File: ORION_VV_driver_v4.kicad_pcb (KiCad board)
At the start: 4 copper layers, 52.4 x 123.1 mm, 154 parts, among them J1 Conn_01x01, J10 Conn_01x01, J11 Conn_01x02, J12 Conn_01x05, J13 Conn_01x05, J14 Conn_01x01, J15 Conn_01x02, J16 Conn_01x01, J17 Conn_01x01, J18 Conn_01x01, J19 Conn_01x01, J2 Conn_01x04, J3 Conn_01x04, J4 Conn_01x06, J5 Conn_01x07, J6 Conn_01x07, J7 Conn_01x01, J8 Conn_01x01, J9 Conn_01x01, Q1 IRF8721PBF-1, Q10 IRF8721PBF-1, Q11 IRF8721PBF-1, Q12 IRF8721PBF-1, Q2 IRF8721PBF-1, Q3 IRF8721PBF-1, Q4 IRF8721PBF-1, Q5 IRF8721PBF-1, Q6 IRF8721PBF-1, Q7 IRF8721PBF-1, Q8 IRF8721PBF-1, Q9 IRF8721PBF-1, SW1 SW_Push, SW2 SW_Push, SW3 SW_Push, SW4 SW_Push, SW5 SW_Push, U1 BD9G101G, U2 L78L33_SOT89, U3 MAX3051, U5 ZXCT108x, U6 ZXCT108x, Y1 Resonator

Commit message: DRC通ってるか！？？！？
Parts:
- SW1, SW2, SW3, SW4, SW5: footprint Button_Switch_SMD:SW_Push_1P1T_NO_CK_KMR2 -> Button_Switch_SMD:SW_Push_SPST_NO_Alps_SKRK
- moved R7 1.80 mm to (115.5, 109.8)
- moved C52 0.94 mm to (108.7, 90.6)
- moved R11 0.82 mm to (113.0, 90.5)
- moved C16 0.81 mm to (113.0, 89.5)
- moved Y1 0.81 mm to (109.5, 107.5)
- turned SW2 to 90 degrees
- turned SW3 to 90 degrees
- turned SW4 to 90 degrees
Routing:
- net GND: track 169.4 -> 203.9 mm, vias 164 -> 176
- net +3V3: track 166.8 -> 187.3 mm, vias 4 -> 5
- net /LED_0: track 1.74 -> 15.6 mm
- net /LED_1: track 1.24 -> 12.8 mm
- net /LED_2: track 0.57 -> 12.0 mm
- net +BATT: track 59.4 -> 48.2 mm, vias 19 -> 18
- net /SW3: track 34.5 -> 29.6 mm
- net /NRST: track 43.4 -> 38.9 mm
- net /SW1: track 37.5 -> 33.5 mm
- net /SW0: track 40.5 -> 36.7 mm
- net /SW2: track 35.4 -> 32.1 mm
- net +9V: track 192.7 -> 195.9 mm, vias 9 -> 10
- net /BATT_V_SENS: track 9.55 -> 8.23 mm
- net /M1_CS: track 35.2 -> 34.1 mm
- net Net-(R7-Pad2): track 8.42 -> 7.26 mm
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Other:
- board text added: "V4.3"
- board text removed: "V4.2"

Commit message: パワー系チェック用のテストパッド追加
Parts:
- added J20: Conn_01x01, TestPoint:TestPoint_Loop_D2.60mm_Drill0.9mm_Beaded, F.Cu at (137.5, 94.5)
- added J21: Conn_01x01, TestPoint:TestPoint_Loop_D2.60mm_Drill0.9mm_Beaded, F.Cu at (137.5, 105.5)
- added J22: Conn_01x01, TestPoint:TestPoint_Loop_D2.60mm_Drill0.9mm_Beaded, F.Cu at (131.0, 130.5)
- added J23: Conn_01x01, TestPoint:TestPoint_Loop_D2.60mm_Drill0.9mm_Beaded, F.Cu at (131.0, 69.5)
- SW1, SW2, SW3, SW4, SW5: footprint Button_Switch_SMD:SW_Push_SPST_NO_Alps_SKRK -> Button_Switch_SMD:SW_Push_1P1T_NO_CK_KMR2
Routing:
- net GND: track 203.9 -> 274.1 mm, vias 176 -> 178
- net /SW0: track 36.7 -> 0.00 mm, vias 1 -> 0
- net /SW1: track 33.5 -> 0.00 mm, vias 1 -> 0
- net /M1_CSL: vias 169 -> 163
- net /M0_CSL: vias 168 -> 162
- added copper zone on B.Cu, net +BATT
- added copper zone on In1.Cu, net +BATT
- added copper zone on In2.Cu, net +BATT

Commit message: 盆栽
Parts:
- SW1, SW2, SW3, SW4, SW5: footprint Button_Switch_SMD:SW_Push_1P1T_NO_CK_KMR2 -> Button_Switch_SMD:SW_Push_SPST_NO_Alps_SKRK
- moved SW2 1.75 mm to (118.5, 128.0)
- moved SW3 1.75 mm to (115.0, 128.0)
- moved SW4 1.75 mm to (111.5, 128.0)
- moved SW5 1.75 mm to (108.0, 128.0)
- moved R10 0.40 mm to (119.5, 92.4)
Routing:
- net GND: track 274.1 -> 204.3 mm, vias 178 -> 176
- net /SW0: track 0.00 -> 35.1 mm, vias 0 -> 1
- net /SW1: track 0.00 -> 32.1 mm, vias 0 -> 1
- net /SW2: track 32.1 -> 30.1 mm
- net /M0_CSL: track 5.91 -> 7.31 mm
- net +9V: track 195.9 -> 197.0 mm
- net /SW3: track 29.6 -> 28.9 mm

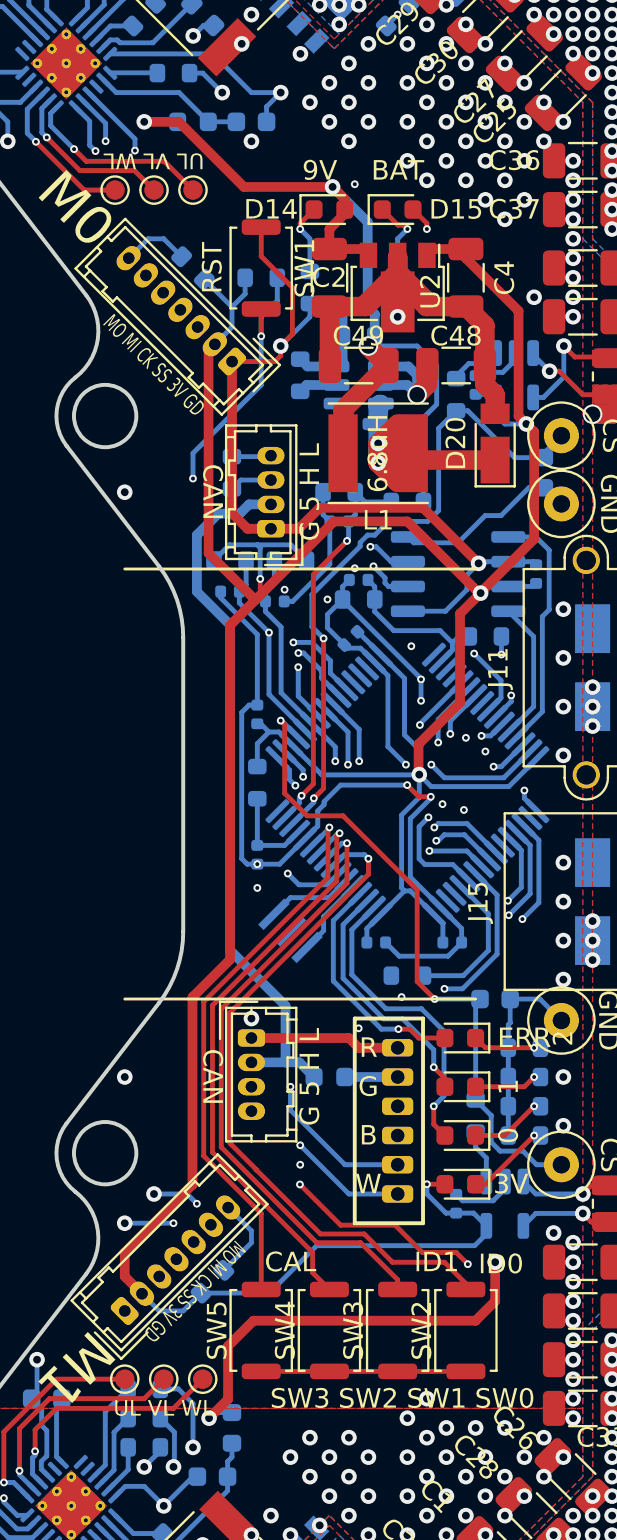
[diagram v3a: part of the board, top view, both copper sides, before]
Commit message: エンコーダ電源にFB追加、GD電源に0Ω抵抗追加
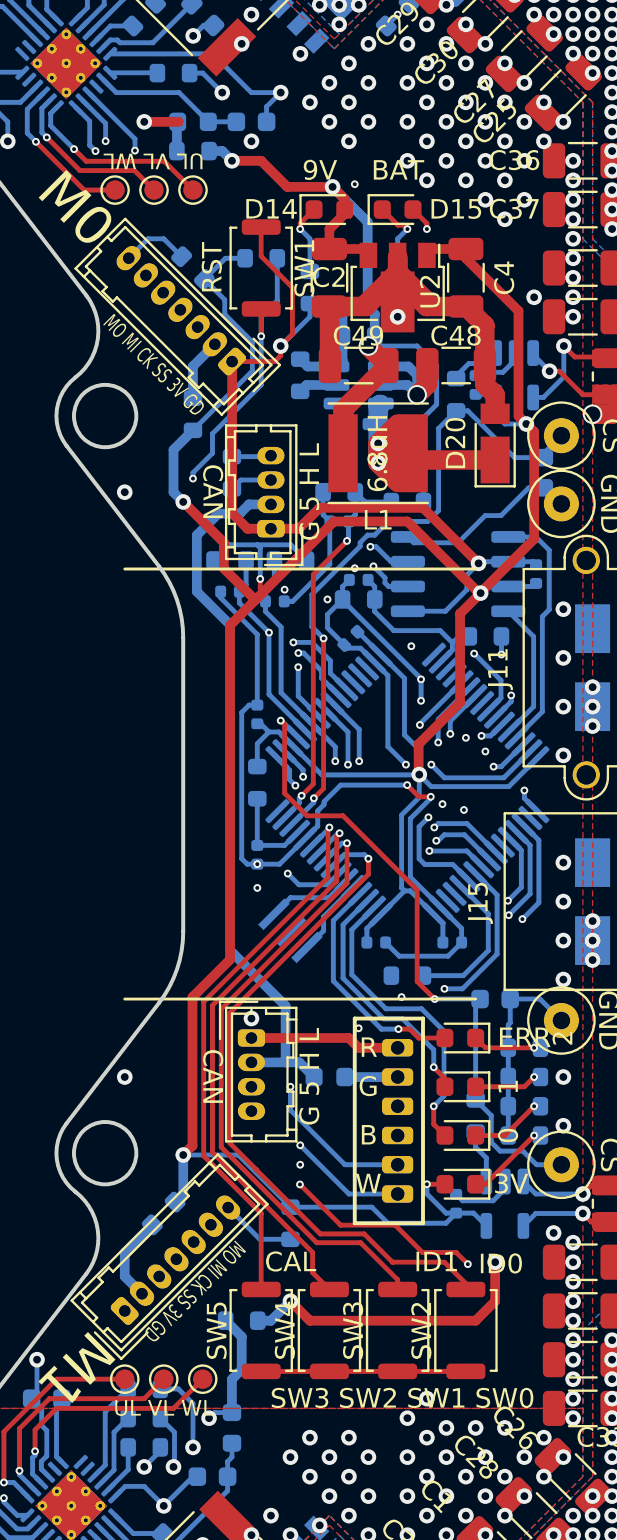
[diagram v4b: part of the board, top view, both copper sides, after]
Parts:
- added FB2: FB100, Resistor_SMD:R_0603_1608Metric, B.Cu at (103.0, 122.0)
- added FB3: FB100, Resistor_SMD:R_0603_1608Metric, B.Cu at (104.5, 81.0)
- added R12: 0, Resistor_SMD:R_0603_1608Metric, B.Cu at (107.0, 127.5)
- added R13: 0, Resistor_SMD:R_0603_1608Metric, B.Cu at (104.5, 67.5)
- moved R15 5.00 mm to (109.5, 122.5), turned to 90 degrees
- moved R5 1.00 mm to (108.0, 73.0)
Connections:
- C12 pad 2: +9V -> /GD_9V_M1
- C13 pad 2: +9V -> /GD_9V_M0
- D10 pad 2: +9V -> /GD_9V_M0
- D11 pad 2: +9V -> /GD_9V_M0
- D6 pad 2: +9V -> /GD_9V_M1
- D7 pad 2: +9V -> /GD_9V_M1
- D8 pad 2: +9V -> /GD_9V_M1
- D9 pad 2: +9V -> /GD_9V_M0
- GD1 pad 4: +9V -> /GD_9V_M1
- GD2 pad 4: +9V -> /GD_9V_M0
- J5 pad 2: +3V3 -> Net-(J5-Pad2)
- J6 pad 2: +3V3 -> Net-(J6-Pad2)
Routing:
- net +9V: track 197.0 -> 116.3 mm, vias 10 -> 5
- net /GD_9V_M1: track 0.00 -> 40.6 mm, vias 0 -> 3
- net /GD_9V_M0: track 0.00 -> 39.3 mm, vias 0 -> 4
- net +3V3: track 187.3 -> 179.9 mm, vias 5 -> 7
- net GND: track 204.3 -> 199.4 mm, vias 176 -> 172
- net Net-(J5-Pad2): track 0.00 -> 4.49 mm
- net Net-(J6-Pad2): track 0.00 -> 3.23 mm
- net /NRST: track 38.9 -> 39.9 mm

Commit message: 銅線貼り付けパターンの改善
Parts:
- moved U5 2.06 mm to (118.5, 122.0)
- moved C15 1.58 mm to (116.5, 122.0)
- moved C48 1.50 mm to (116.5, 78.5)
- moved C49 1.50 mm to (111.5, 78.5)
- moved R16 1.12 mm to (109.5, 74.0)
- moved R5 1.12 mm to (107.5, 74.0)
- moved C14 1.00 mm to (118.0, 79.5)
- moved C46 1.00 mm to (112.0, 81.5)
- moved R32 1.00 mm to (109.0, 79.0)
- moved R33 1.00 mm to (112.0, 77.0)
- moved R9 1.00 mm to (117.0, 80.0)
- moved U1 1.00 mm to (112.0, 79.5)
- moved U6 1.00 mm to (120.0, 79.0)
- moved C47 0.98 mm to (112.0, 75.5)
- moved C2 0.50 mm to (111.0, 74.0)
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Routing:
- net +BATT: track 47.9 -> 53.1 mm
- net /M1_CSL: track 6.00 -> 8.20 mm
- net /GD_9V_M0: track 39.3 -> 37.5 mm
- net GND: track 199.4 -> 200.9 mm
- net +3V3: track 179.9 -> 178.5 mm
- net /NRST: track 39.9 -> 38.7 mm
- net +9V: track 116.3 -> 115.2 mm
- net Net-(R8-Pad2): track 2.77 -> 3.64 mm
- net Net-(C46-Pad1): track 13.8 -> 14.6 mm
- net /M0_CS: track 33.6 -> 34.3 mm
- net /M0_CSL: track 7.31 -> 7.97 mm
- net /GD_V_SENS: track 20.3 -> 19.8 mm
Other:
- board text added: "V4.4"
- board text removed: "V4.3"

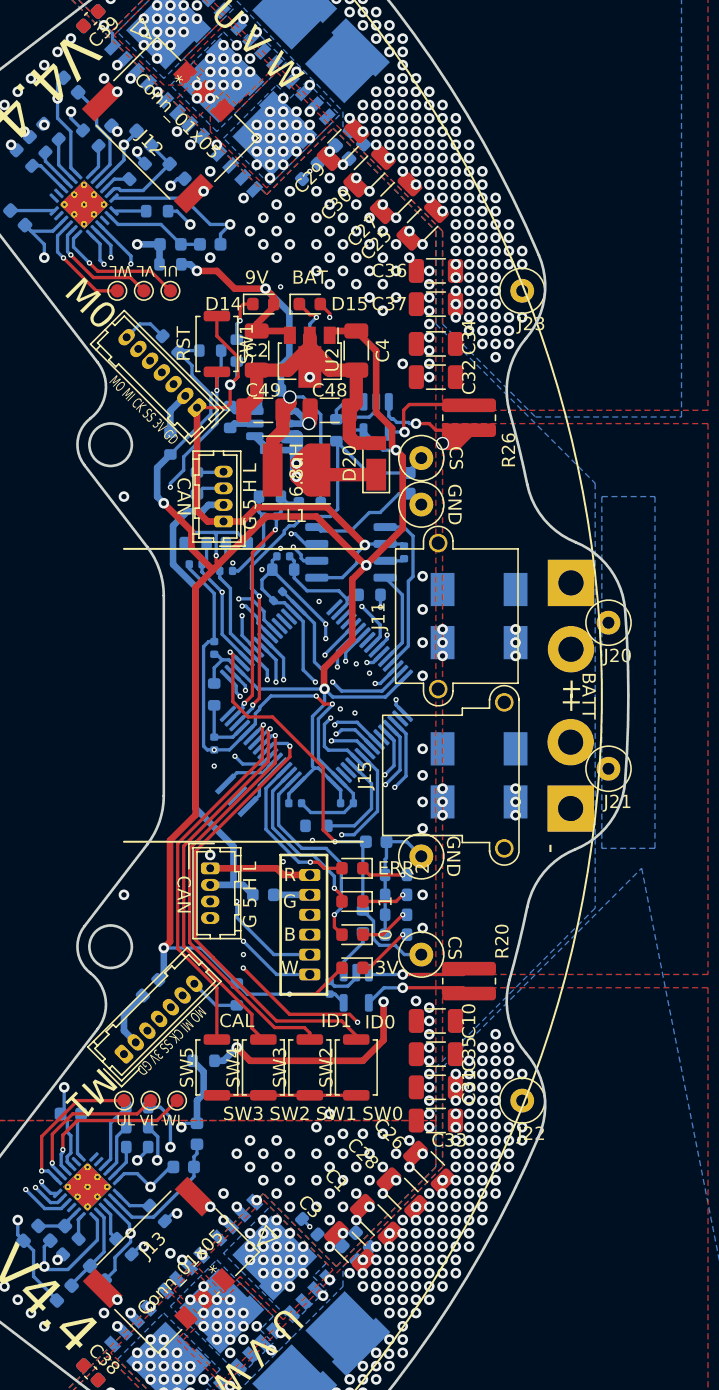
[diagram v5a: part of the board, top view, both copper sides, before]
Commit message: 判別用シルク追加
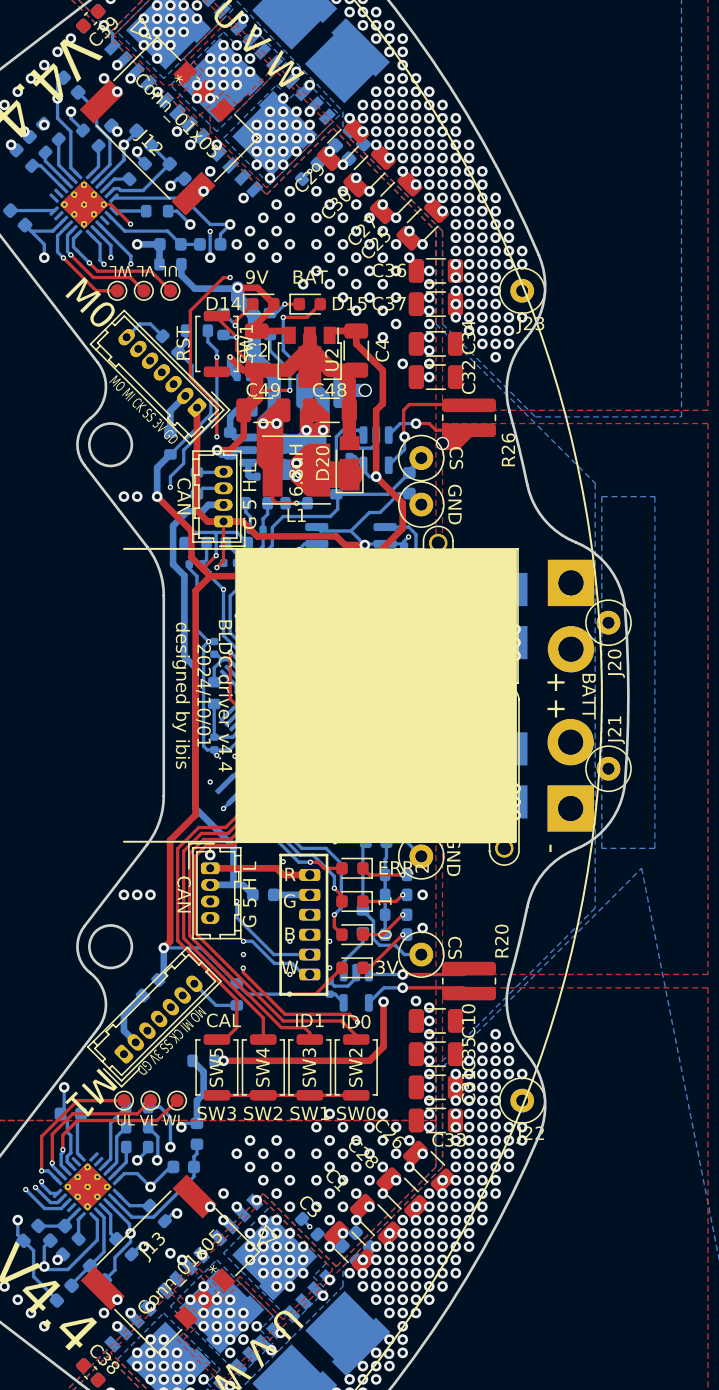
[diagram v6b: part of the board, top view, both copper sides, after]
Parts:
- removed FB1, FB2, FB3: FB100, Resistor_SMD:R_0603_1608Metric
- added C53: 0.1u, Capacitor_SMD:C_0402_1005Metric, B.Cu at (110.0, 76.0)
- added C54: 0.1u, Capacitor_SMD:C_0402_1005Metric, B.Cu at (110.0, 75.0)
- added F1: Polyfuse, Fuse:Fuse_1210_3225Metric, B.Cu at (116.0, 77.0)
- added R38: 0, Resistor_SMD:R_0603_1608Metric, B.Cu at (103.0, 122.0)
- added R39: 0, Resistor_SMD:R_0603_1608Metric, B.Cu at (104.5, 81.0)
- added R40: 1, Resistor_SMD:R_0603_1608Metric, B.Cu at (107.8, 99.8)
- R20, R26: value 10m -> 5m
- moved R9 4.00 mm to (117.0, 84.0)
- moved R17 3.91 mm to (112.0, 72.0)
- moved U6 2.50 mm to (120.0, 81.5)
- moved R16 2.24 mm to (108.5, 72.0)
- moved C46 2.06 mm to (111.5, 83.5)
- moved U1 2.06 mm to (111.5, 81.5)
- moved C14 2.00 mm to (118.0, 81.5)
- moved D20 2.00 mm to (118.0, 82.5)
- moved R32 2.00 mm to (109.0, 81.0)
- moved R5 1.80 mm to (106.5, 72.5)
- moved C47 1.58 mm to (111.5, 77.0)
- moved R33 1.58 mm to (111.5, 78.5)
- moved C50 1.41 mm to (111.0, 87.5)
- moved R35 1.12 mm to (111.0, 85.5)
- moved R34 1.00 mm to (114.0, 85.5)
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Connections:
- C48 pad 1: +BATT -> +24V
- U1 pad 4: +BATT -> +24V
- U1 pad 5: +BATT -> +24V
- U4 pad 50: unconnected-(U4-Pad50) -> /LED_A
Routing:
- net +24V: track 0.00 -> 24.3 mm, vias 0 -> 2
- net GND: track 200.9 -> 222.8 mm, vias 172 -> 198
- net +9V: track 115.2 -> 125.7 mm, vias 5 -> 6
- net +BATT: track 53.1 -> 45.8 mm
- net /M0_CS: track 34.3 -> 30.3 mm
- net /SW3: track 28.9 -> 31.7 mm
- net +3V3: track 178.5 -> 175.8 mm
- net Net-(R9-Pad2): track 2.99 -> 5.08 mm
- net /M0_VL: track 47.4 -> 45.4 mm
- net /M0_WL: track 46.8 -> 44.8 mm
- net Net-(C46-Pad1): track 14.6 -> 16.4 mm
- net /M0_CSL: track 7.97 -> 9.77 mm
- net Net-(D15-Pad1): track 4.08 -> 2.49 mm
- net /TEMP_FET_0: track 49.5 -> 51.1 mm, vias 3 -> 4
- net /NRST: track 38.7 -> 40.1 mm
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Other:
- board text added: "BLDC driver v4.4 2024/10/01 designed by ibis"
